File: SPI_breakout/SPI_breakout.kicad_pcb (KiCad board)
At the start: 2 copper layers, 45.8 x 38 mm, 13 parts, among them J1 OPC-N3 A, J2 OPC-N3 B, J3 External OPC 5V Input, J4 Jumper, U2 MicroSD

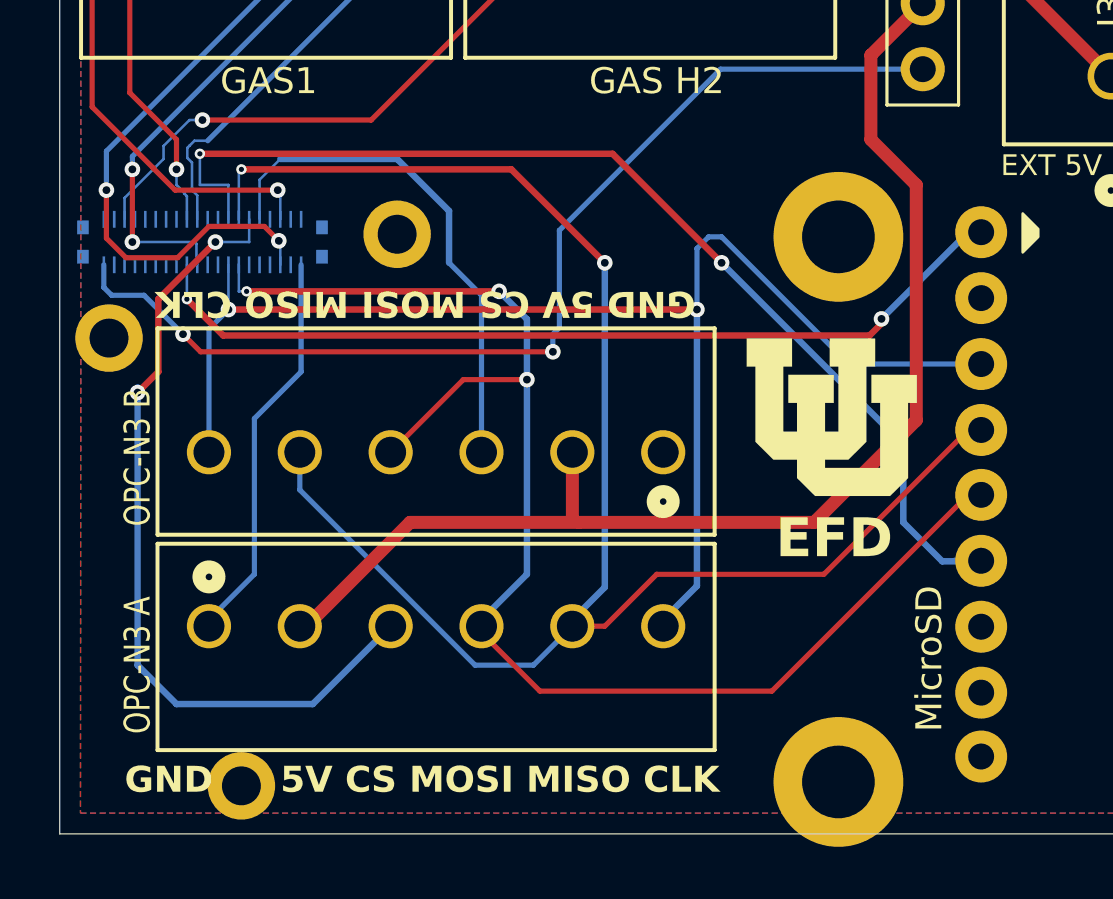
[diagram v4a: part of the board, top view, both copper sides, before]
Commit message: Change IO pin to 2 to avoid GPS conflict
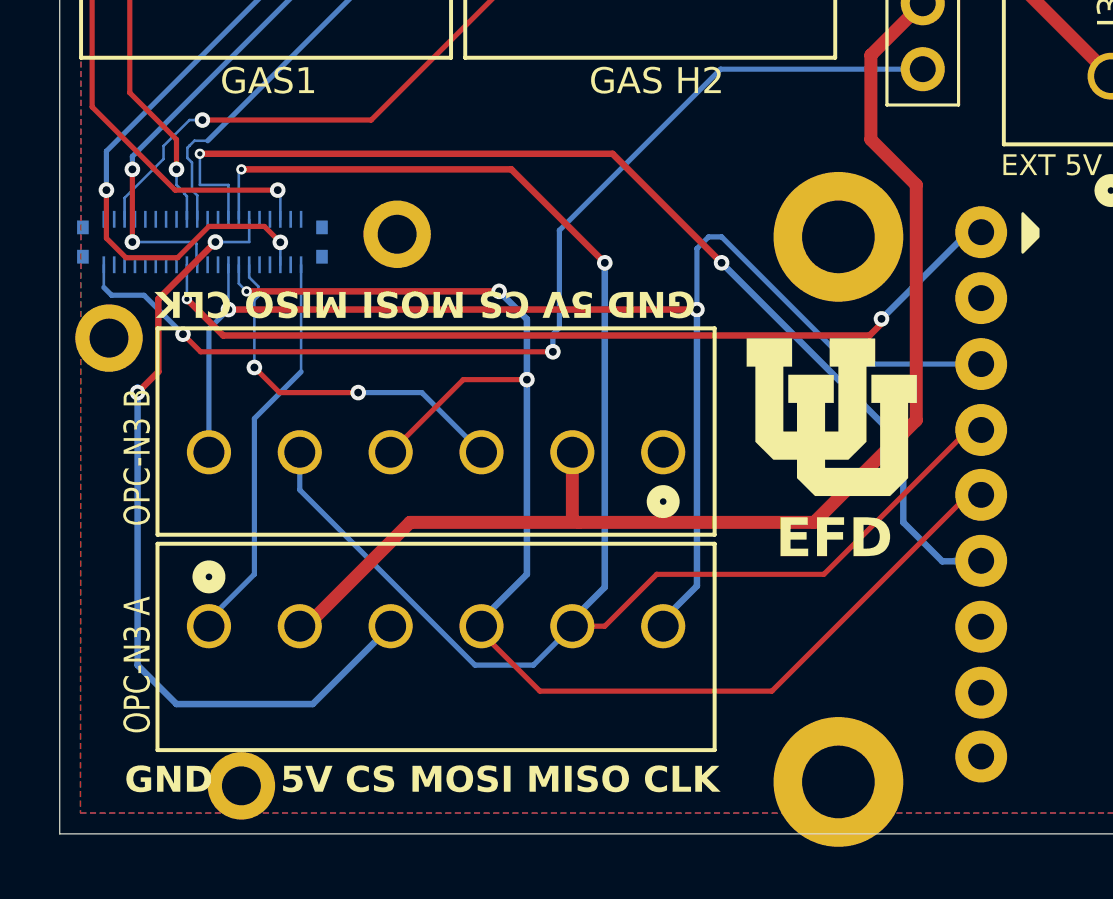
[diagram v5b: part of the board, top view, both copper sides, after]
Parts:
- U2: value MicroSD -> ~
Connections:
- U1 pad 30: unconnected-(U1-IO2-Pad30) -> /OPC2_CS
- U1 pad 31: /OPC2_CS -> unconnected-(U1-IO3-Pad31)
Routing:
- net /OPC2_CS: track 19.8 -> 14.3 mm, vias 0 -> 2

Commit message: Final checks
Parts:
- J3: footprint MyParts:CONN_1935161_PXC -> Connector_Phoenix_MC:PhoenixContact_MC_1,5_2-G-3.81_1x02_P3.81mm_Horizontal
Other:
- board text added: "5V EXT"
- board text added: "OPC H"
- board text added: "OPC L"
- board text added: "VBAT"
